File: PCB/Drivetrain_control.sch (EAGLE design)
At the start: 27 parts, among them IC1 LM358N, J1 SSW-110-02-G-S, J2 SSW-110-02-G-S, J3 SSW-110-02-G-S, J4 SSW-110-02-G-S, J5 SSW-110-02-G-S, J6 SSW-110-02-G-S, J7 SSW-110-02-G-S, J8 SSW-110-02-G-S, Q1 IRFI540NPBF, Q2 IRFI540NPBF, Q3 IRFI540NPBF, Q4 IRFI540NPBF, Q5 IRFI540NPBF

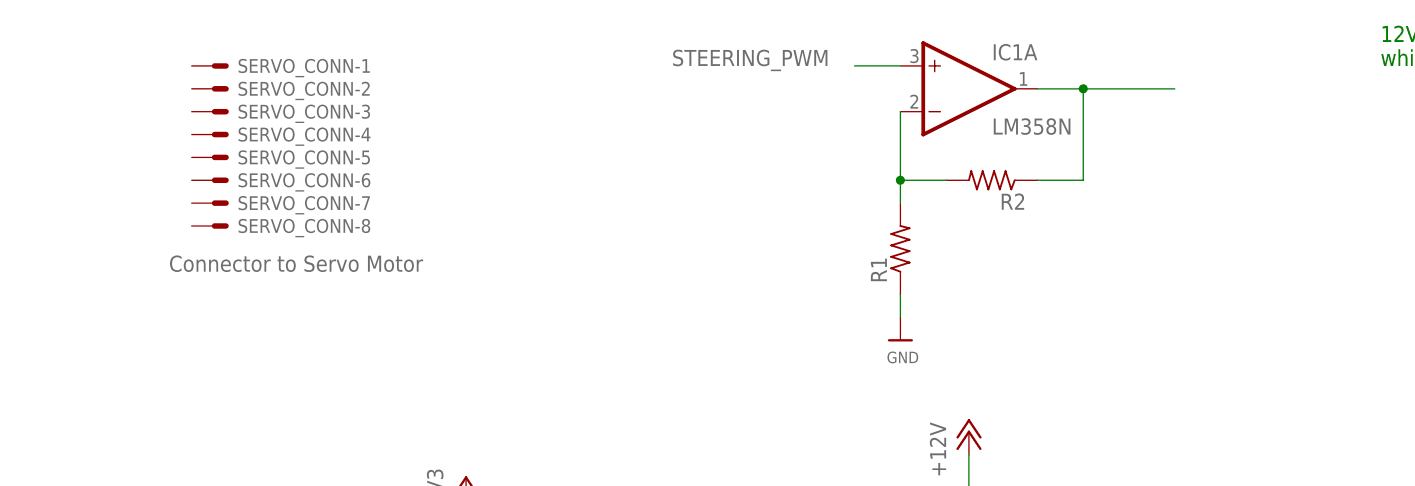
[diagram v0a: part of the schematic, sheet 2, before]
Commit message: Added outputs to servo connector
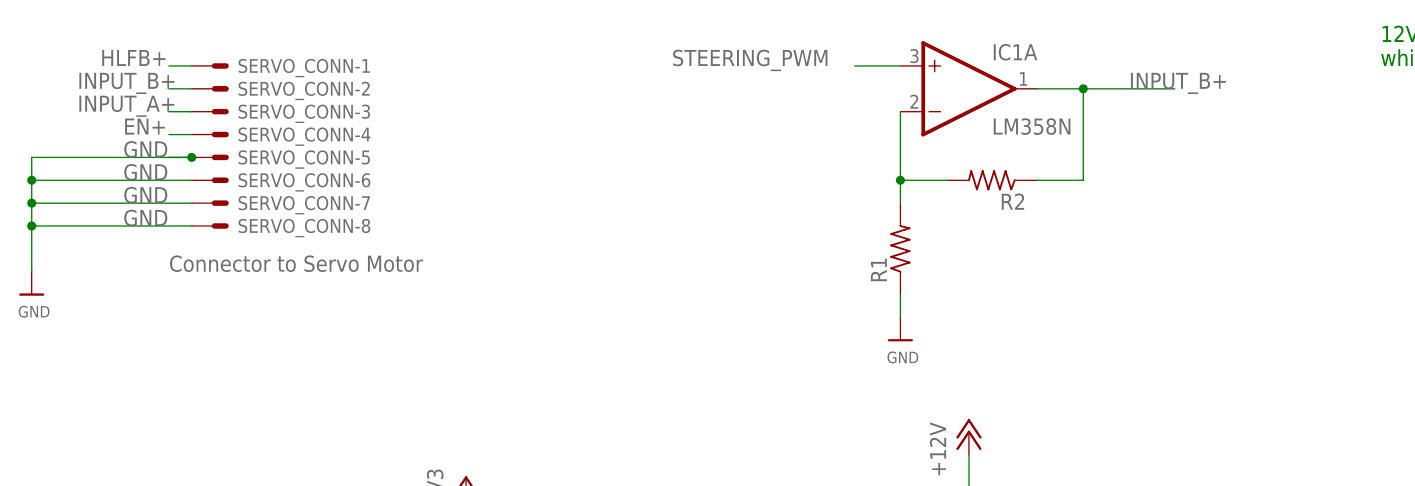
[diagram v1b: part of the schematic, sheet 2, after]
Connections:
- removed net N$4: IC1A.OUT, R2.1
- new net EN+: SERVO_CONN-4.S
- new net HLFB+: SERVO_CONN-1.S
- new net INPUT_A+: SERVO_CONN-3.S
- new net INPUT_B+: IC1A.OUT, R2.1, SERVO_CONN-2.S
- net GND: now also SERVO_CONN-5.S, SERVO_CONN-6.S, SERVO_CONN-7.S, SERVO_CONN-8.S
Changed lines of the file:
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@@
 <?xml version="1.0" encoding="utf-8"?>
 <!DOCTYPE eagle SYSTEM "eagle.dtd">
-<eagle version="9.3.0">
+<eagle version="9.3.2">
 <drawing>
 <settings>
@@
 <part name="P+2" library="supply1" library_urn="urn:adsk.eagle:library:371" deviceset="+5V" device=""/>
 <part name="GND3" library="supply1" library_urn="urn:adsk.eagle:library:371" deviceset="GND" device=""/>
+<part name="U$8" library="microbuilder" deviceset="GND" device=""/>
 </parts>
 <sheets>
@@
 <attribute name="NAME" x="68.58" y="86.868" size="1.778" layer="95" font="vector"/>
 </instance>
+<instance part="U$8" gate="G$1" x="15.24" y="172.72" smashed="yes">
+<attribute name="VALUE" x="13.716" y="170.18" size="1.27" layer="96"/>
+</instance>
 </instances>
 <busses>
@@
 <wire x1="137.16" y1="139.7" x2="137.16" y2="124.46" width="0.1524" layer="91"/>
 </segment>
+<segment>
+<pinref part="SERVO_CONN" gate="-5" pin="S"/>
+<wire x1="33.02" y1="187.96" x2="30.48" y2="187.96" width="0.1524" layer="91"/>
+<label x="25.4" y="187.96" size="1.778" layer="95"/>
+<pinref part="U$8" gate="G$1" pin="GND"/>
+<wire x1="33.02" y1="187.96" x2="15.24" y2="187.96" width="0.1524" layer="91"/>
+<wire x1="15.24" y1="187.96" x2="15.24" y2="185.42" width="0.1524" layer="91"/>
+<junction x="33.02" y="187.96"/>
+<pinref part="SERVO_CONN" gate="-6" pin="S"/>
+<wire x1="15.24" y1="185.42" x2="15.24" y2="182.88" width="0.1524" layer="91"/>
+<label x="25.4" y="185.42" size="1.778" layer="95"/>
+<wire x1="15.24" y1="182.88" x2="15.24" y2="180.34" width="0.1524" layer="91"/>
+<wire x1="15.24" y1="180.34" x2="15.24" y2="175.26" width="0.1524" layer="91"/>
+<wire x1="33.02" y1="185.42" x2="15.24" y2="185.42" width="0.1524" layer="91"/>
+<junction x="15.24" y="185.42"/>
+<pinref part="SERVO_CONN" gate="-7" pin="S"/>
+<label x="25.4" y="182.88" size="1.778" layer="95"/>
+<wire x1="33.02" y1="182.88" x2="15.24" y2="182.88" width="0.1524" layer="91"/>
+<junction x="15.24" y="182.88"/>
+<pinref part="SERVO_CONN" gate="-8" pin="S"/>
+<label x="25.4" y="180.34" size="1.778" layer="95"/>
+<wire x1="33.02" y1="180.34" x2="15.24" y2="180.34" width="0.1524" layer="91"/>
+<junction x="15.24" y="180.34"/>
+</segment>
 </net>
 <net name="N$2" class="0">
@@
 <wire x1="132.08" y1="134.62" x2="144.78" y2="134.62" width="0.1524" layer="91"/>
 <junction x="132.08" y="134.62"/>
-</segment>
-</net>
-<net name="N$4" class="0">
-<segment>
-<pinref part="IC1" gate="A" pin="OUT"/>
-<wire x1="127" y1="195.58" x2="132.08" y2="195.58" width="0.1524" layer="91"/>
-<pinref part="R2" gate="G$1" pin="1"/>
-<wire x1="132.08" y1="195.58" x2="132.08" y2="185.42" width="0.1524" layer="91"/>
-<wire x1="132.08" y1="185.42" x2="127" y2="185.42" width="0.1524" layer="91"/>
-<wire x1="132.08" y1="195.58" x2="142.24" y2="195.58" width="0.1524" layer="91"/>
-<junction x="132.08" y="195.58"/>
 </segment>
 </net>
@@
 </segment>
 </net>
+<net name="EN+" class="0">
+<segment>
+<pinref part="SERVO_CONN" gate="-4" pin="S"/>
+<wire x1="33.02" y1="190.5" x2="30.48" y2="190.5" width="0.1524" layer="91"/>
+<label x="25.4" y="190.5" size="1.778" layer="95"/>
+</segment>
+</net>
+<net name="INPUT_A+" class="0">
+<segment>
+<pinref part="SERVO_CONN" gate="-3" pin="S"/>
+<wire x1="33.02" y1="193.04" x2="30.48" y2="193.04" width="0.1524" layer="91"/>
+<label x="20.32" y="193.04" size="1.778" layer="95"/>
+</segment>
+</net>
+<net name="INPUT_B+" class="0">
+<segment>
+<pinref part="SERVO_CONN" gate="-2" pin="S"/>
+<wire x1="33.02" y1="195.58" x2="30.48" y2="195.58" width="0.1524" layer="91"/>
+<label x="20.32" y="195.58" size="1.778" layer="95"/>
+</segment>
+<segment>
+<pinref part="IC1" gate="A" pin="OUT"/>
+<wire x1="127" y1="195.58" x2="132.08" y2="195.58" width="0.1524" layer="91"/>
+<pinref part="R2" gate="G$1" pin="1"/>
+<wire x1="132.08" y1="195.58" x2="132.08" y2="185.42" width="0.1524" layer="91"/>
+<wire x1="132.08" y1="185.42" x2="127" y2="185.42" width="0.1524" layer="91"/>
+<wire x1="132.08" y1="195.58" x2="142.24" y2="195.58" width="0.1524" layer="91"/>
+<junction x="132.08" y="195.58"/>
+<label x="137.16" y="195.58" size="1.778" layer="95"/>
+</segment>
+</net>
+<net name="HLFB+" class="0">
+<segment>
+<pinref part="SERVO_CONN" gate="-1" pin="S"/>
+<wire x1="33.02" y1="198.12" x2="30.48" y2="198.12" width="0.1524" layer="91"/>
+<label x="22.86" y="198.12" size="1.778" layer="95"/>
+</segment>
+</net>

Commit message: Preliminary Layout
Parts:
- removed J10: (no value), SparkFun-Connectors:CONN_16
- removed J11: (no value), SparkFun-Connectors:CONN_12
- removed Q2, Q3, Q4, Q5: IRFI540NPBF, transistor-power:IRFI540NPBF
- added BRAKE_CONN: 1X2-3.5MM, adafruit:1X2-3.5MM
- added DCDC_CONN, JETSON_CONN: 22-23-2021, con-molex:22-23-2021
- added MC_CONN: 22-23-2031, con-molex:22-23-2031
- added MS1: FEATHERWING_NODIM, adafruit:FEATHERWING_NODIM
- added Q10, Q6, Q7, Q8, Q9: 100V/17A, SparkFun-DiscreteSemi:MOSFET-NCH-FQP30N06L
- added R5: (no value), resistor:R-US_R0805
- Q1: value IRFI540NPBF -> 220mA/50V/3.5Ω; device transistor-power:IRFI540NPBF -> SparkFun-DiscreteSemi:MOSFET-NCH-BSS138
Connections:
- removed net EN_SERVO: Q1.D
- removed net N$3: IC1A.-IN, R1.2, R2.2
- removed net N$5: Q1.G
- removed net N$6: Q4.G
- removed net N$7: Q2.G
- removed net N$8: Q5.G
- removed net N$9: Q3.G
- new net PWM_12V: Q1.D, R2.1
- new net TI_PWM: Q1.S, R1.1
- net +12V: now also BRAKE_CONN.1, DCDC_CONN-1.S, R2.2, R5.2
- net +3V3: now also JETSON_CONN-1.S, MS1.3V, Q1.G, R1.2
- net BRAKE_SOLENOID: now also BRAKE_CONN.2, Q10.D; no longer Q5.D
- net EN+: now also Q6.D, R5.1
- net FS1_MC: now also MC_CONN-1.S, Q9.D; no longer Q2.D
- net FWD_MC: now also MC_CONN-2.S, Q8.D; no longer Q3.D
- net GND: now also DCDC_CONN-2.S, JETSON_CONN-2.S, MS1.GND, Q10.S, Q6.S, Q7.S, Q8.S, Q9.S; no longer Q1.S, Q2.S, Q3.S, Q4.S, Q5.S, R1.1
- net INPUT_B+: no longer IC1A.OUT, R2.1
- net REV_MC: now also MC_CONN-3.S, Q7.D; no longer Q4.D
- net STEERING_PWM: no longer IC1A.+IN
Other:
- note removed: "+3V3"
- note removed: "12"
- note removed: "13"
- note removed: "A0"
- note removed: "A1"
- note removed: "A2"
- note removed: "A3"
- note removed: "A4"
- note removed: "A5"
- note removed: "AREF"
- note removed: "EN"
- note removed: "IO1"
- note removed: "MISO"
- note removed: "MOSI"
- note removed: "RST"
- note removed: "SCK"
- note removed: "SCL"
- note removed: "SDA"
- note removed: "USB"
- note removed: "VBAT"
- note removed: "~10"
- note removed: "~11"
- note removed: "~5"
- note removed: "~6"
- note removed: "~9"
- moved on the sheet: R1, R2

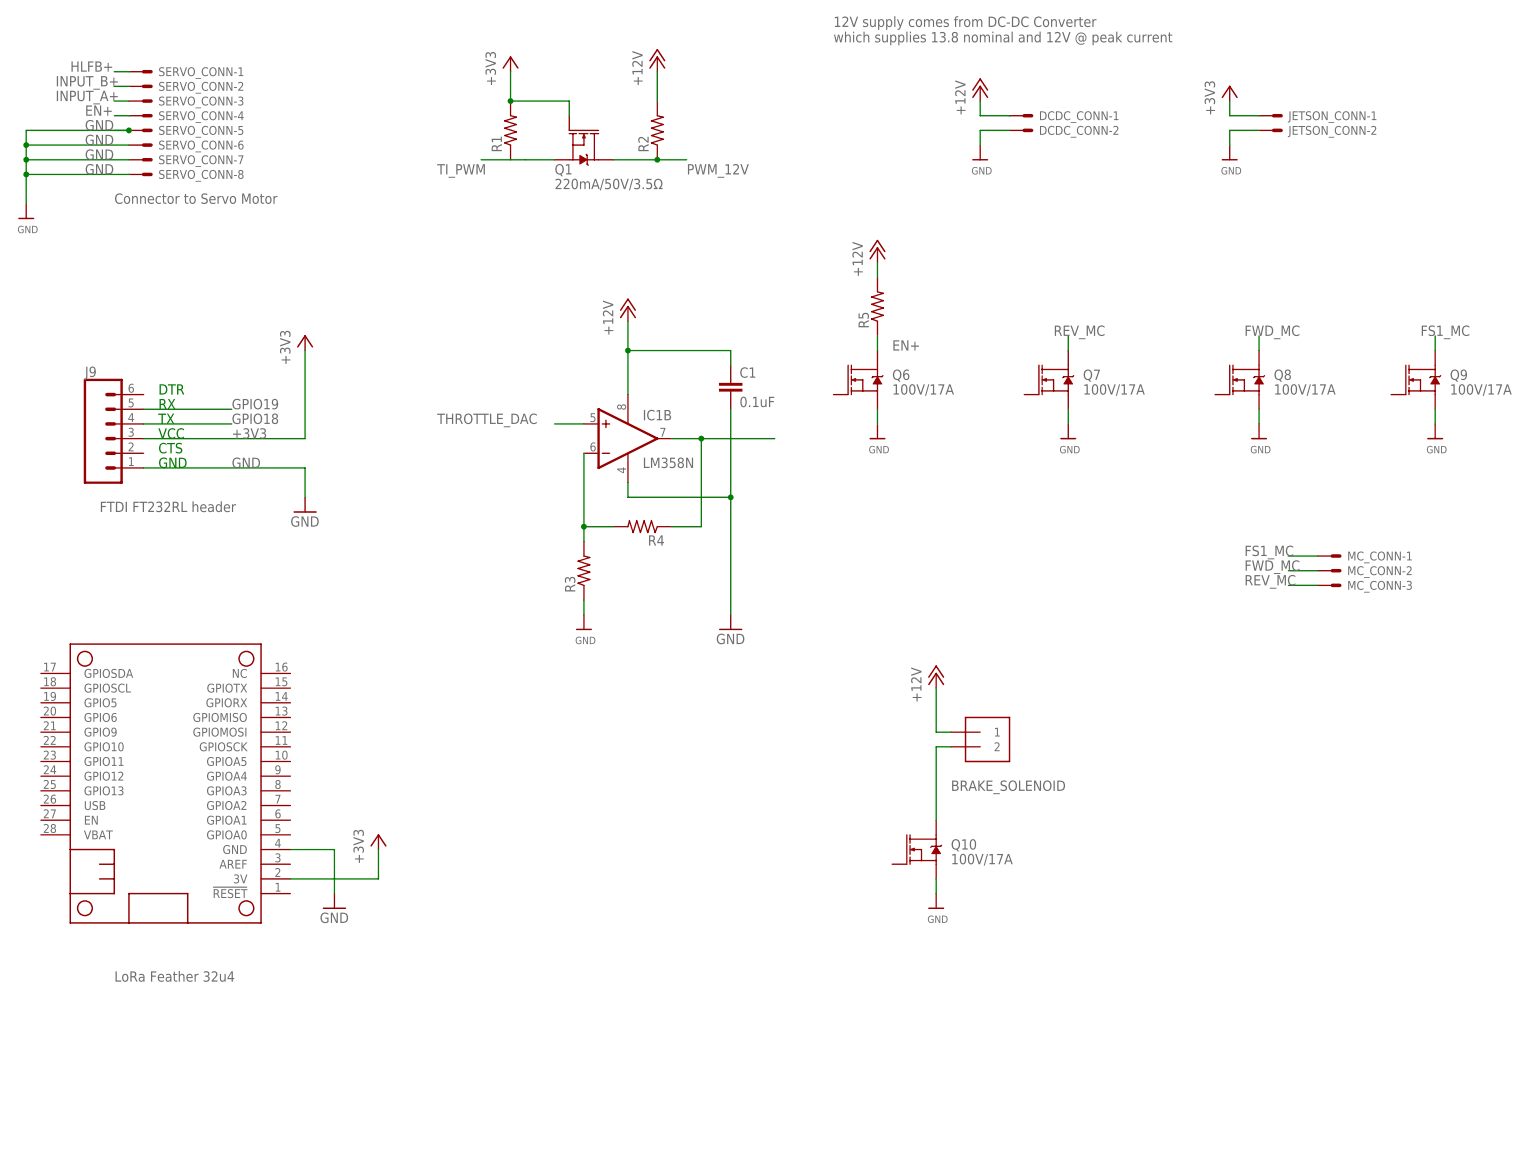
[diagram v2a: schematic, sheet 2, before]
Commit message: Feather pins added
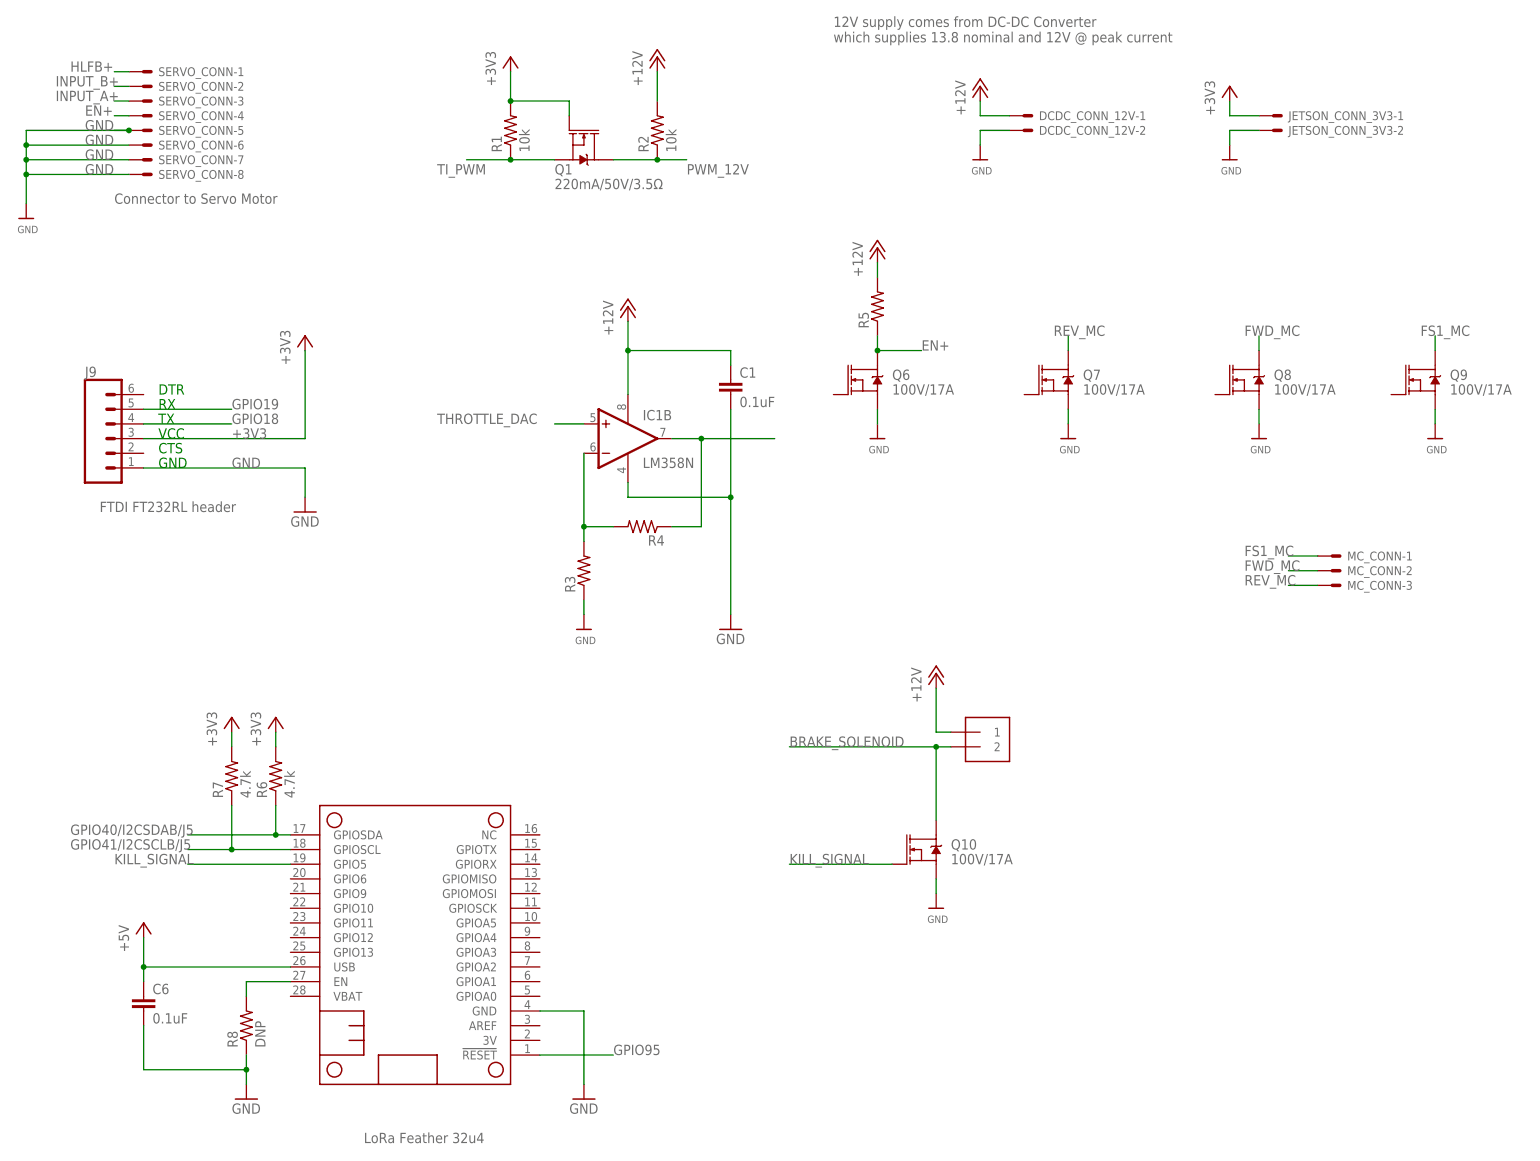
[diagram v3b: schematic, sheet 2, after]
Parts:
- added C6: 0.1uF, eagle-ltspice:C
- added R6, R7: 4.7k, resistor:R-US_R0805
- added R8: DNP, resistor:R-US_R0805
- R1, R2: value (none) -> 10k
- renumbered DCDC_CONN to DCDC_CONN_12V, JETSON_CONN to JETSON_CONN_3V3
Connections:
- new net KILL_SIGNAL: MS1.GPIO5, Q10.G
- new net N$3: MS1.EN, R8.2
- net +3V3: now also R6.2, R7.2; no longer MS1.3V
- net +5V: now also C6.1, MS1.USB
- net GND: now also C6.2, R8.1
- net GPIO40/I2CSDAB/J5: now also MS1.GPIOSDA, R6.1
- net GPIO41/I2CSCLB/J5: now also MS1.GPIOSCL, R7.1
- net GPIO95: now also MS1.!RESET

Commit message: Finished Schematic and Routing, Version 1.0
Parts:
- removed J9: (no value), SparkFun-Connectors:CONN_06LONGPADS
- removed JETSON_CONN_3V3: 22-23-2021, con-molex:22-23-2021
- added D1: 1N4004, diode:1N4004
- added ENCODER_CONN, JETSON_CONN_PWR: 22-23-2031, con-molex:22-23-2031
- added FTDI: (no value), SparkFun-Connectors:CONN_06LONGPADS
- added Q2: 100V/17A, SparkFun-DiscreteSemi:MOSFET-NCH-FQP30N06L
- added R10, R11, R12, R13, R14, R15, R16, R17, R18, R9: (no value), resistor:R-US_R0805
- MC_CONN: value 22-23-2031 -> 22-23-2041; device con-molex:22-23-2031 -> con-molex:22-23-2041
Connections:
- net GPIO40/I2CSDAB/J5 renamed I2CSDAB
- net GPIO41/I2CSCLB/J5 renamed I2CSCLB
- net GPIO95 renamed FEATHER_RESET
- removed net GPIO10/PWMOUT6A: J8-6.1
- removed net GPIO11/PWMOUT6B: J8-5.1
- removed net GPIO14/OPXBAR3: J8-4.1
- removed net GPIO16/OPXBAR7: J4-3.1
- removed net GPIO18: J1-4.1, J9.4
- removed net GPIO19: J1-3.1, J9.5
- removed net GPIO24/OPXBAR1: J4-4.1
- removed net GPIO6/PWMOUT4A: J8-10.1
- removed net GPIO7/PWMOUT4B: J8-9.1
- removed net GPIO8/PWMOUT5A: J8-8.1
- removed net GPIO9/PWMOUT5B: J8-7.1
- removed net PWM_12V: Q1.D, R2.1
- new net EN+_CTL: J4-4.1, Q6.G
- new net ENCODER_U: ENCODER_CONN-1.S, R12.2
- new net ENCODER_V: ENCODER_CONN-2.S, R11.2
- new net ENCODER_W: ENCODER_CONN-3.S, R10.2
- new net FS1_CTL: J8-10.1, Q9.G
- new net FWD_CTL: J8-9.1, Q8.G
- new net INPUT_A+_CTL: J4-3.1, Q2.G
- new net MC_HLFB+: J8-4.1, R16.1, R17.2
- new net MC_U: J8-7.1, R12.1, R15.2
- new net MC_V: J8-6.1, R11.1, R14.2
- new net MC_W: J8-5.1, R10.1, R13.2
- new net REV_CTL: J8-8.1, Q7.G
- new net SCIB_RX: FTDI.5, J1-3.1
- new net SCIB_TX: FTDI.4, J1-4.1
- new net THROTTLE_MC: IC1B.OUT, MC_CONN-4.S, R4.1
- net +12V: now also R18.2, R9.2
- net +3V3: now also FTDI.3, JETSON_CONN_PWR-2.S; no longer J9.3, JETSON_CONN_3V3-1.S
- net +5V: now also JETSON_CONN_PWR-1.S
- net BRAKE_SOLENOID: now also D1.A
- net GND: now also FTDI.1, JETSON_CONN_PWR-3.S, Q2.S, R13.1, R14.1, R15.1, R17.1; no longer J9.1, JETSON_CONN_3V3-2.S
- net HLFB+: now also R16.2
- net INPUT_A+: now also Q2.D, R18.1
- net INPUT_B+: now also Q1.D, R2.1
- net N$2: now also D1.C, R9.1; no longer IC1B.OUT, R4.1
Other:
- moved on the sheet: C1, DCDC_CONN_12V-1, DCDC_CONN_12V-2, IC1B, MC_CONN-1, MC_CONN-2, MC_CONN-3, Q6, Q7, Q8, R3, R4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

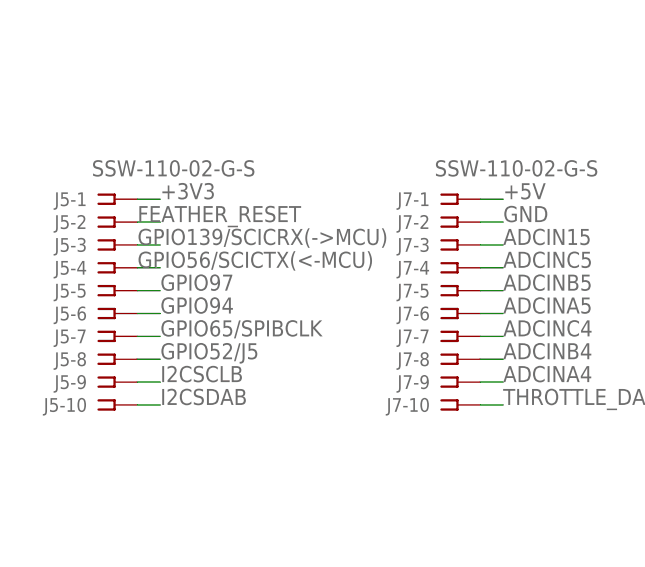
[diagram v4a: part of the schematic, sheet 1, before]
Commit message: Added Kill Signal route to GPIO pin of TI
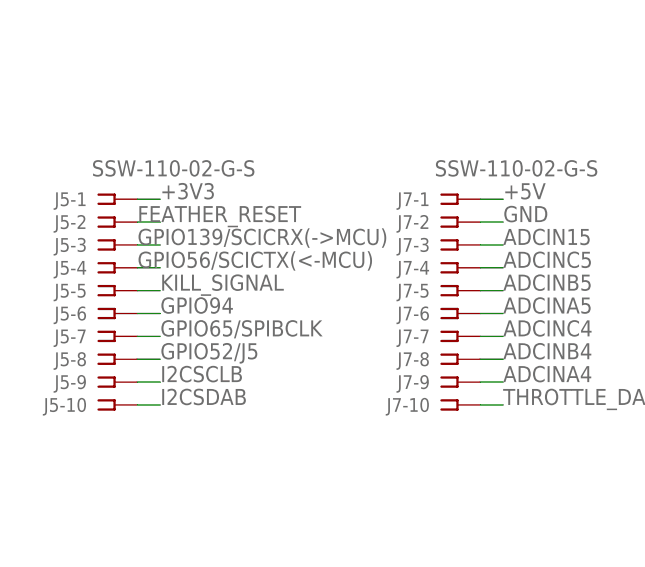
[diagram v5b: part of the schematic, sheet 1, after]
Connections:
- removed net GPIO97: J5-5.1
- net KILL_SIGNAL: now also J5-5.1
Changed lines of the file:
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@@
 </segment>
 </net>
-<net name="GPIO97" class="0">
+<net name="KILL_SIGNAL" class="0">
 <segment>
 <pinref part="J5" gate="-5" pin="1"/>
@@
 <instance part="JETSON_CONN_PWR" gate="-1" x="241.3" y="187.96" smashed="yes">
 <attribute name="NAME" x="243.84" y="187.198" size="1.524" layer="95"/>
-<attribute name="VALUE" x="240.538" y="189.357" size="1.778" layer="96"/>
 </instance>
 <instance part="JETSON_CONN_PWR" gate="-2" x="241.3" y="185.42" smashed="yes">
